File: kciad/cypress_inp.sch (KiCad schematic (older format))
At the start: 57 parts, among them J1 Cypress CY7C68013A Left Bot, J10 Conn_01x03_Male, J11 Conn_01x03_Male, J2 Connector PDx, J3 Cypress CY7C68013A Right Bot, J4 Connector PBx, J5 Power, J6 USB_B, J7 Conn_01x04_Male, J8 Conn_01x03_Male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

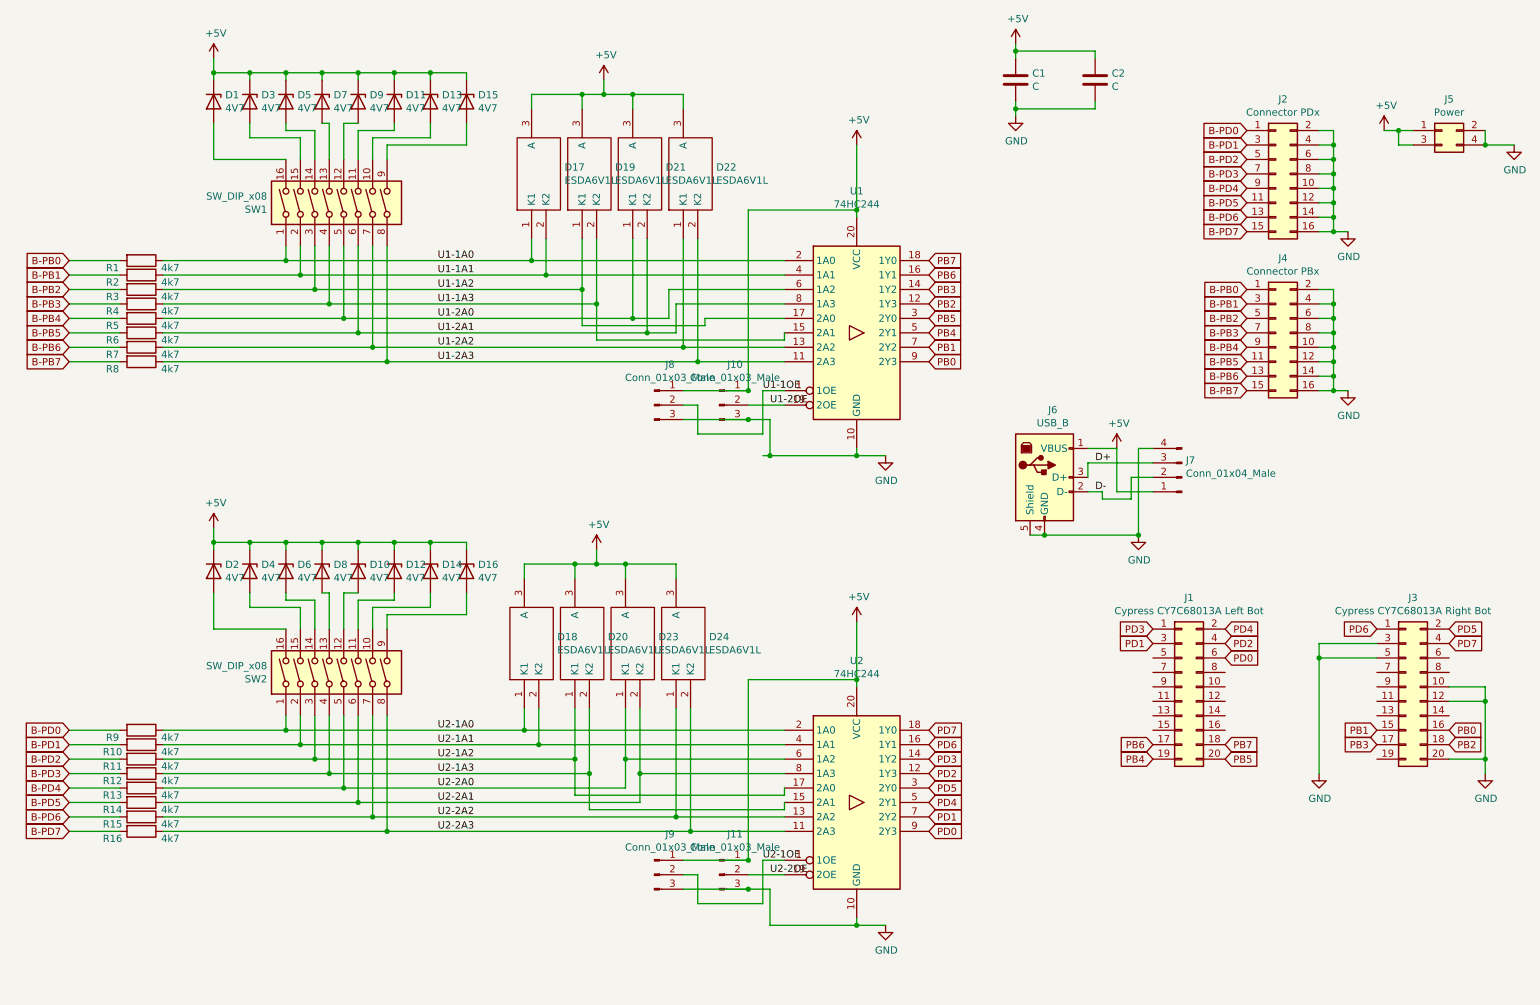
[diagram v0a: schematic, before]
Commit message: * changed whole schematic and pcb layout
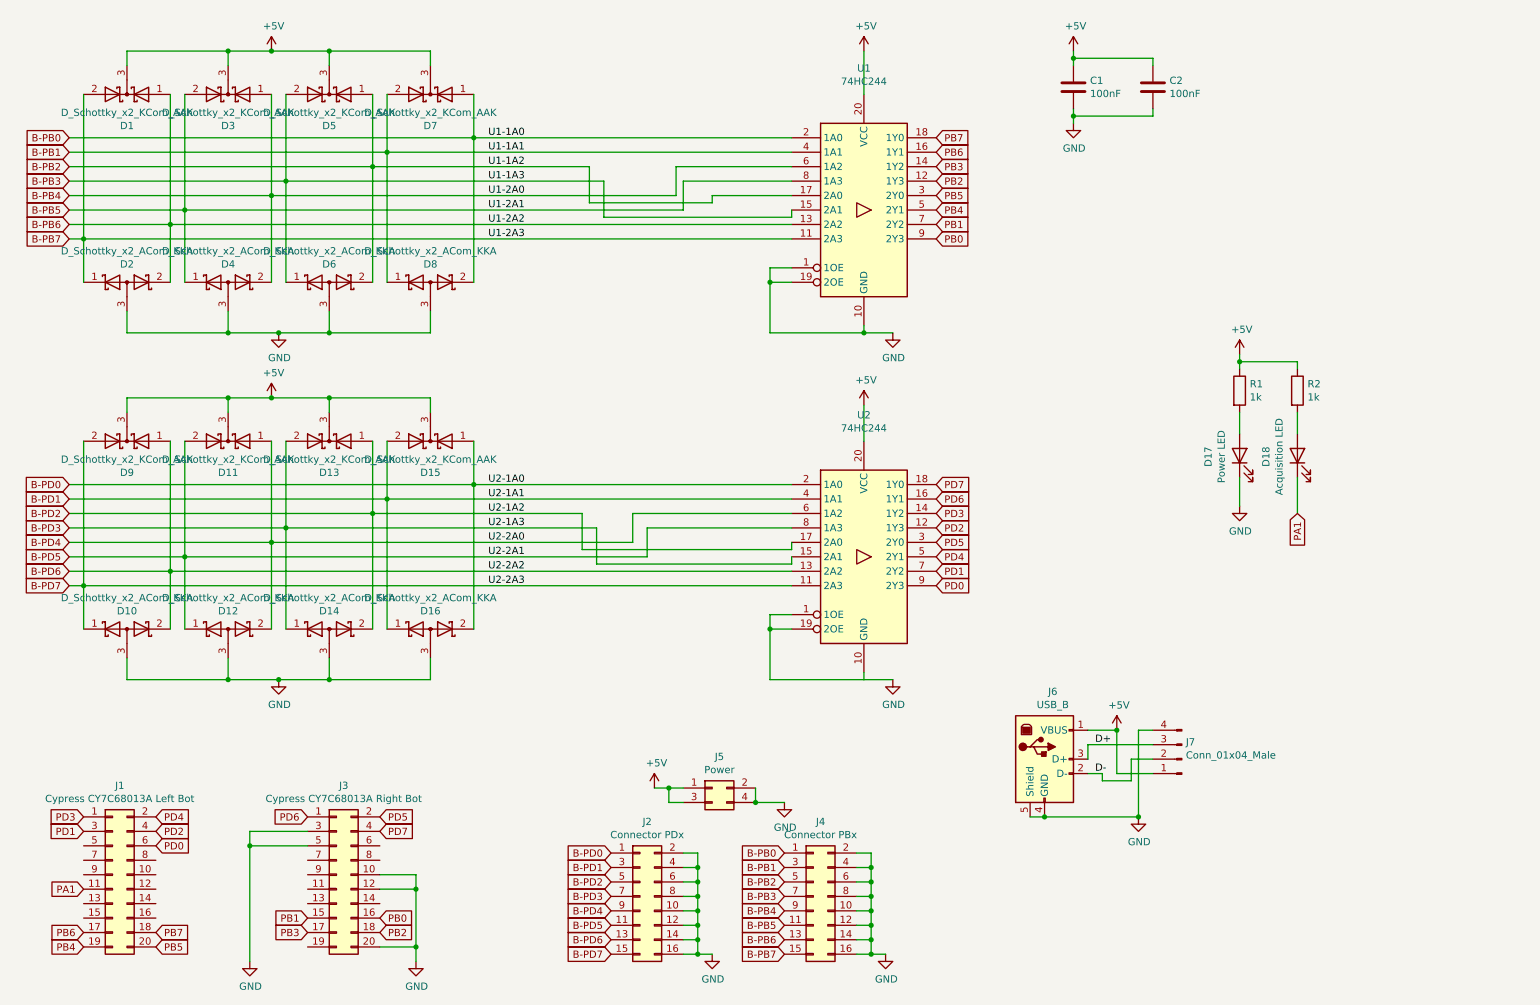
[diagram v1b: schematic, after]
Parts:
- removed D1, D10, D11, D12, D13, D14, D15, D16, D2, D3, D4, D5, D6, D7, D8, D9: 4V7, Diode_THT:D_DO-34_SOD68_P7.62mm_Horizontal, symbol Device:D_Zener
- removed D17, D18, D19, D20, D21, D22, D23, D24: ESDA6V1L, SamacSys_Parts:SOT105P242X150-3N, symbol cypress_inp-rescue:ESDA6V1L-SamacSys_Parts
- removed J10, J11, J8, J9: Conn_01x03_Male, Connector_PinHeader_2.54mm:PinHeader_1x03_P2.54mm_Vertical, symbol Connector:Conn_01x03_Male
- removed R10, R11, R12, R13, R14, R15, R16, R3, R4, R5, R6, R7, R8, R9: 4k7, Resistor_THT:R_Axial_DIN0204_L3.6mm_D1.6mm_P7.62mm_Horizontal, symbol Device:R
- removed SW1, SW2: SW_DIP_x08, Button_Switch_THT:SW_DIP_SPSTx08_Slide_9.78x22.5mm_W7.62mm_P2.54mm, symbol Switch:SW_DIP_x08
- added D1, D11, D13, D15, D3, D5, D7, D9: D_Schottky_x2_KCom_AAK, Package_TO_SOT_SMD:SOT-23_Handsoldering, symbol Device:D_Schottky_x2_KCom_AAK
- added D10, D12, D14, D16, D2, D4, D6, D8: D_Schottky_x2_ACom_KKA, Package_TO_SOT_SMD:SOT-23_Handsoldering, symbol Device:D_Schottky_x2_ACom_KKA
- added D17: Power LED, LED_THT:LED_D3.0mm, symbol Device:LED
- added D18: Acquisition LED, LED_THT:LED_D3.0mm, symbol Device:LED
- C1, C2: value C -> 100nF; footprint Capacitor_THT:C_Disc_D4.7mm_W2.5mm_P5.00mm -> Capacitor_SMD:C_1206_3216Metric_Pad1.33x1.80mm_HandSolder
- R1, R2: value 4k7 -> 1k; footprint Resistor_THT:R_Axial_DIN0204_L3.6mm_D1.6mm_P7.62mm_Horizontal -> Resistor_SMD:R_1210_3225Metric_Pad1.30x2.65mm_HandSolder
- U1, U2: footprint Package_DIP:DIP-20_W7.62mm_Socket -> Package_SO:SO-20_5.3x12.6mm_P1.27mm
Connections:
- net U1-1A2 is gone; now on net B-PB2: U1.17 (2A0)
- net U1-1A3 is gone; now on net B-PB3: U1.15 (2A1)
- net U1-1OE is gone; now on net GND: U1.1 (1OE)
- net U1-2A0 is gone; now on net B-PB4: U1.6 (1A2)
- net U1-2A1 is gone; now on net B-PB5: U1.8 (1A3)
- net U1-2A2 is gone; now on net B-PB6: U1.13 (2A2)
- net U1-2A3 is gone; now on net B-PB7: U1.11 (2A3)
- net U1-2OE is gone; now on net GND: U1.19 (2OE)
- net U2-1A0 is gone; now on net B-PD0: U2.2 (1A0)
- net U2-1A1 is gone; now on net B-PD1: U2.4 (1A1)
- net U2-1A2 is gone; now on net B-PD2: U2.17 (2A0)
- net U2-1A3 is gone; now on net B-PD3: U2.15 (2A1)
- net U2-1OE is gone; now on net GND: U2.1 (1OE)
- net U2-2A0 is gone; now on net B-PD4: U2.6 (1A2)
- net U2-2A1 is gone; now on net B-PD5: U2.8 (1A3)
- net U2-2A2 is gone; now on net B-PD6: U2.13 (2A2)
- net U2-2A3 is gone; now on net B-PD7: U2.11 (2A3)
- net U2-2OE is gone; now on net GND: U2.19 (2OE)
- net +5V: now also R1.1, R2.1, D1.3 (K), D11.3 (K), D13.3 (K), D15.3 (K), D3.3 (K), D5.3 (K), D7.3 (K), D9.3 (K)
- net B-PB0: now also U1.2 (1A0), D7.1 (A), D8.2 (K); no longer R1.2
- net B-PB1: now also U1.4 (1A1), D7.2 (A), D8.1 (K); no longer R2.2
- net B-PB2: now also D5.1 (A), D6.2 (K)
- net B-PB3: now also D5.2 (A), D6.1 (K)
- net B-PB4: now also D3.1 (A), D4.2 (K)
- net B-PB5: now also D3.2 (A), D4.1 (K)
- net B-PB6: now also D1.1 (A), D2.2 (K)
- net B-PB7: now also D1.2 (A), D2.1 (K)
- net B-PD0: now also D15.1 (A), D16.2 (K)
- net B-PD1: now also D15.2 (A), D16.1 (K)
- net B-PD2: now also D13.1 (A), D14.2 (K)
- net B-PD3: now also D13.2 (A), D14.1 (K)
- net B-PD4: now also D11.1 (A), D12.2 (K)
- net B-PD5: now also D11.2 (A), D12.1 (K)
- net B-PD6: now also D10.2 (K), D9.1 (A)
- net B-PD7: now also D10.1 (K), D9.2 (A)
- net GND: now also D10.3 (A), D12.3 (A), D14.3 (A), D16.3 (A), D17.1 (K), D2.3 (A), D4.3 (A), D6.3 (A), D8.3 (A)
- net PA1: now reaches J1.11 (Pin_11)
- net PA1: now also D18.1 (K)
- removed net U1-1A0: R1.1, U1.2 (1A0)
- removed net U1-1A1: R2.1, U1.4 (1A1)
- new net: D17.2 (A), R1.2
- new net: D18.2 (A), R2.2
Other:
- moved on the sheet: C1, C2, J1, J2, J3, J4, J5, J6, J7, U1, U2
